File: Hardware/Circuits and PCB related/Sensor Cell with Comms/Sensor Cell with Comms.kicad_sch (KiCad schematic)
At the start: 5 parts, among them U1 TCAN337

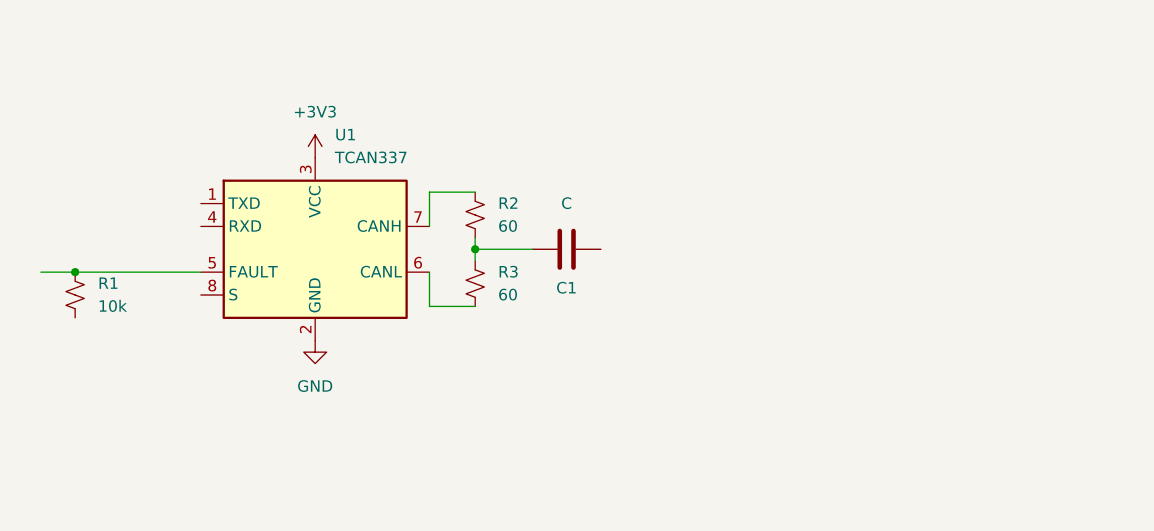
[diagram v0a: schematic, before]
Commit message: TCAN337 Wiring diagram redone to include the componenent sizing for the pcb stage
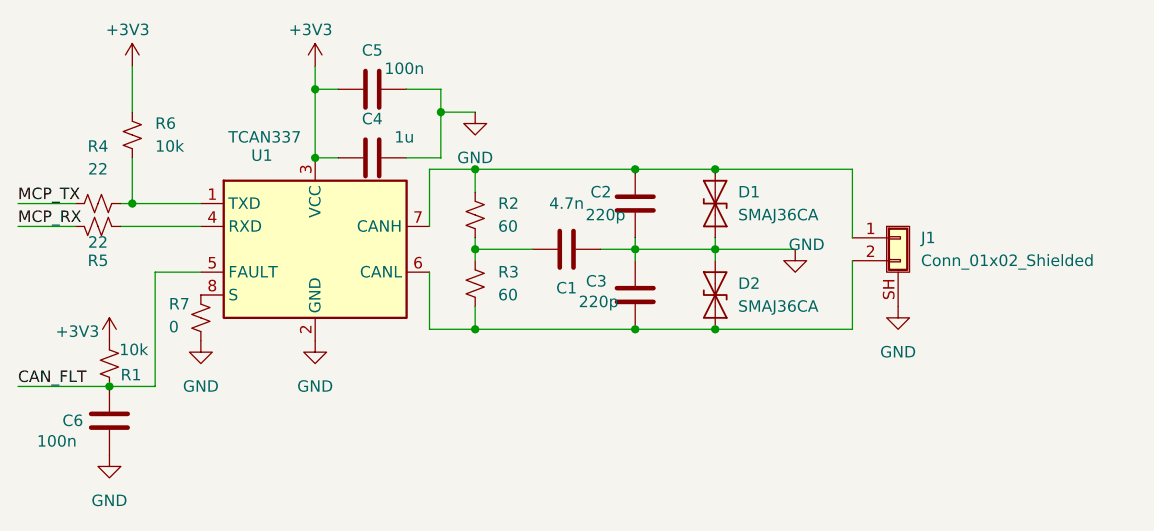
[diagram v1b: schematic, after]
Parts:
- added C2, C3: 220p, Capacitor_SMD:C_0603_1608Metric_Pad1.08x0.95mm_HandSolder, symbol Device:C
- added C4: 1u, Capacitor_SMD:C_0603_1608Metric_Pad1.08x0.95mm_HandSolder, symbol Device:C
- added C5, C6: 100n, Capacitor_SMD:C_0603_1608Metric_Pad1.08x0.95mm_HandSolder, symbol Device:C
- added D1, D2: SMAJ36CA, Diode_SMD:D_SMA, symbol Diode:SMAJ36CA
- added J1: Conn_01x02_Shielded, symbol Connector_Generic_Shielded:Conn_01x02_Shielded
- added R4, R5: 22, Resistor_SMD:R_0603_1608Metric_Pad0.98x0.95mm_HandSolder, symbol Device:R_Small_US
- added R6: 10k, Resistor_SMD:R_0603_1608Metric_Pad0.98x0.95mm_HandSolder, symbol Device:R_Small_US
- added R7: 0, Resistor_SMD:R_0603_1608Metric_Pad0.98x0.95mm_HandSolder, symbol Device:R_Small_US
- C1: value C -> 4.7n
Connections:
- net +3V3: now also R1.1, C4.2, C5.2, R6.2
- net GND: now also C1.2, C2.1, C3.2, C4.1, C5.1, C6.1, D1.1 (A1), D2.2 (A2), J1.SH (Shield), R7.1
- net at R2.1, U1.7 (CANH): now also C2.2, D1.2 (A2), J1.1 (Pin_1)
- net CAN_FLT: now reaches R1.2, U1.5 (FAULT)
- net CAN_FLT: now also C6.2
- net at R3.2, U1.6 (CANL): now also C3.1, D2.1 (A1), J1.2 (Pin_2)
- net at U1.1 (TXD): now also R4.1, R6.1
- net at U1.4 (RXD): now also R5.2
- net at U1.8 (S): now also R7.2
- new net MCP_RX: R5.1
- new net MCP_TX: R4.2
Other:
- moved on the sheet: R1

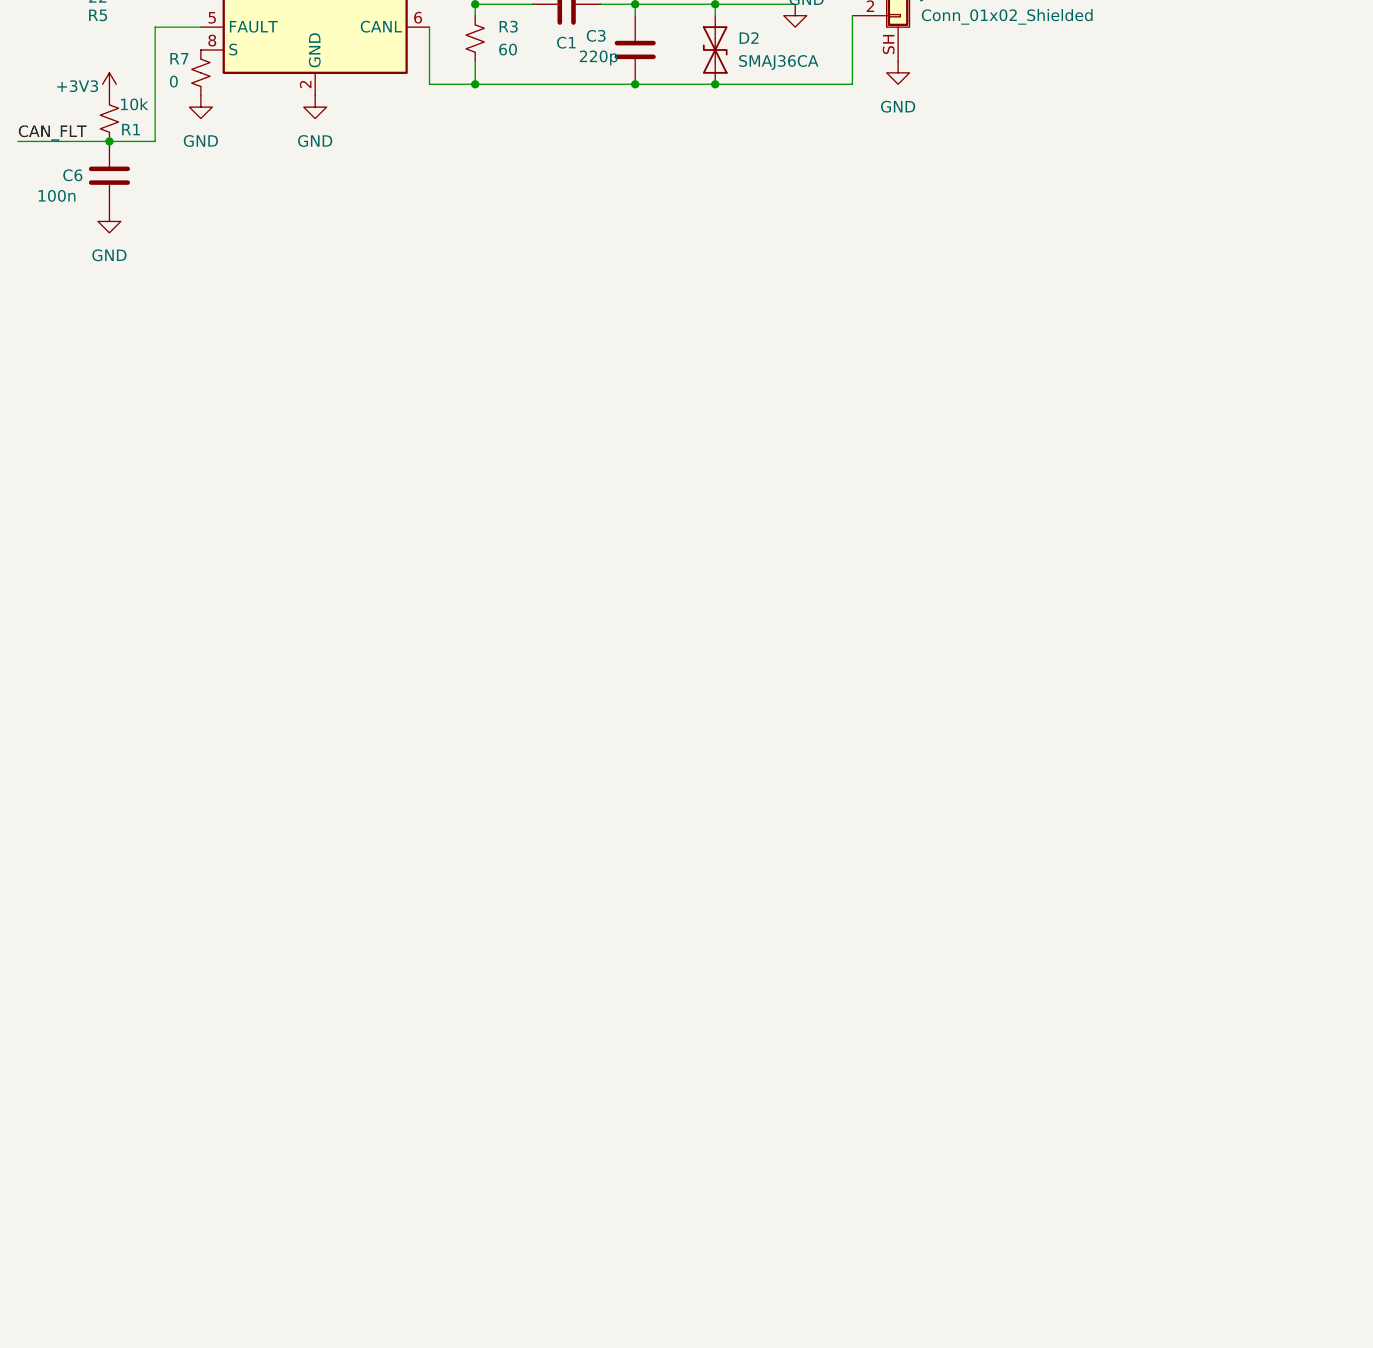
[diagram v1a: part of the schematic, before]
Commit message: need to finish TPS22950x model and wiring but good now for the rest. After wiring diag is done finish actual wiring and move onto PCB process
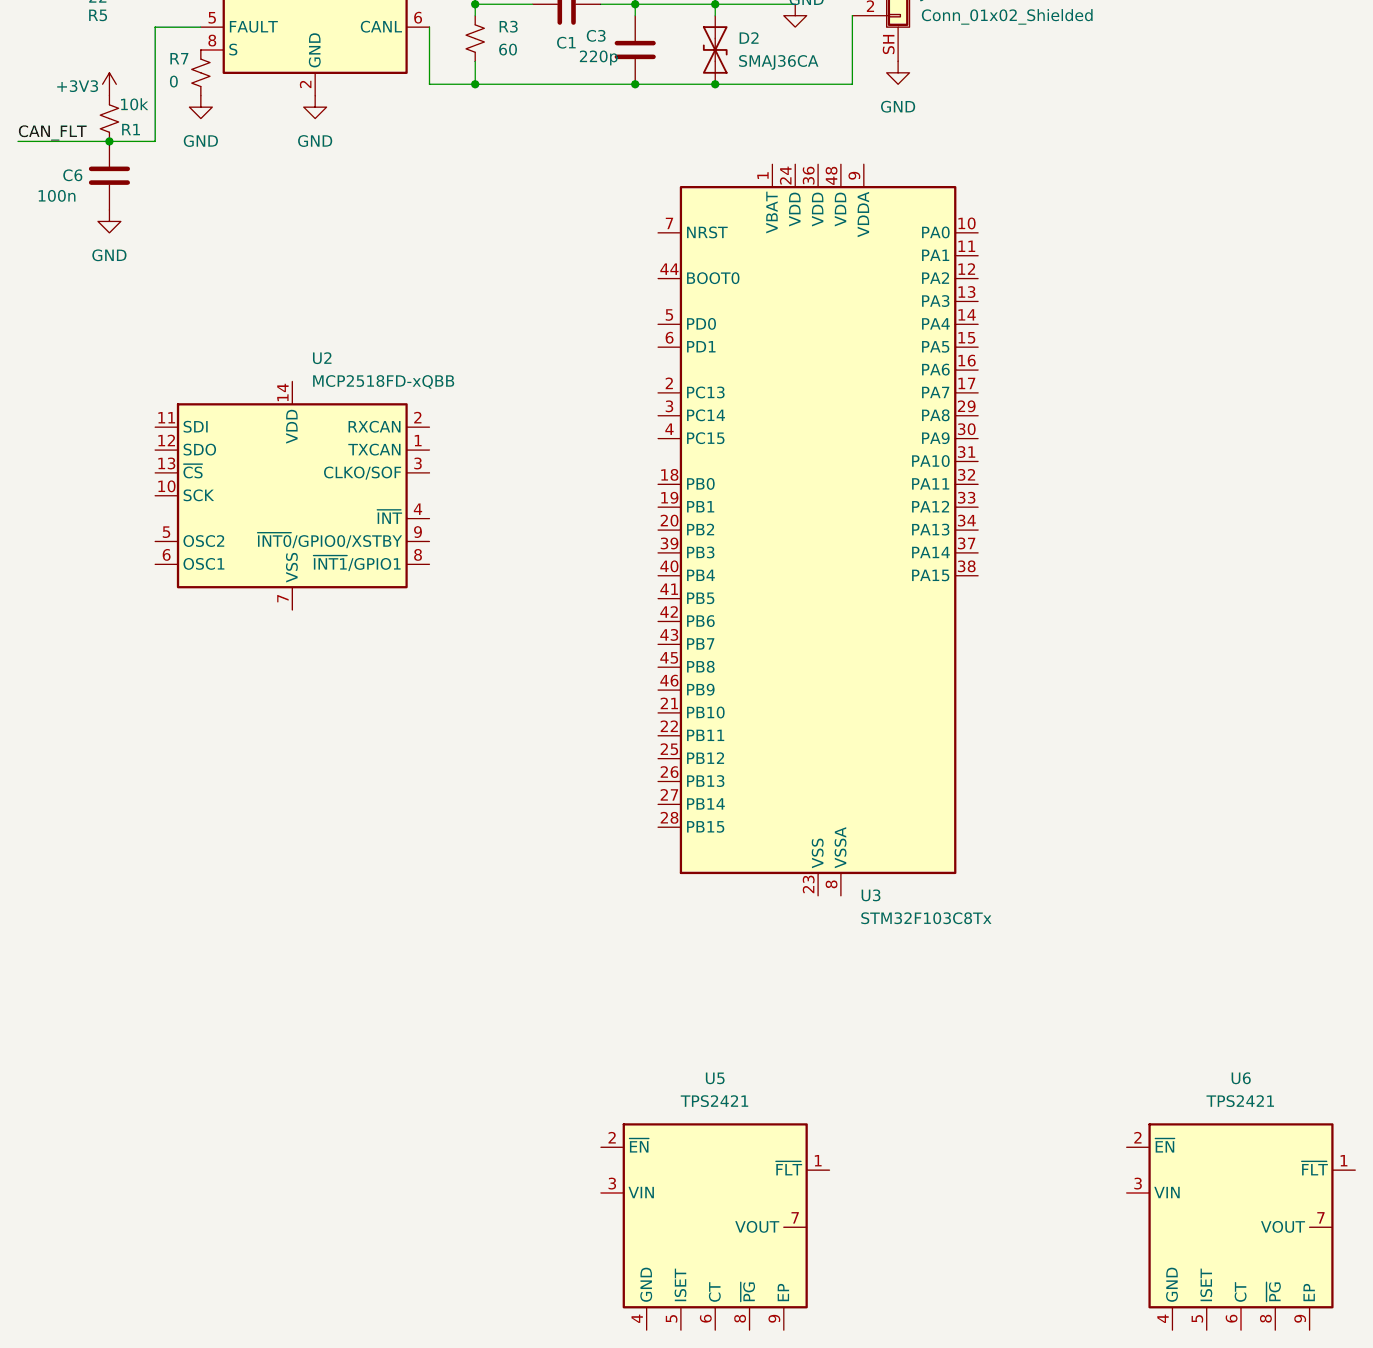
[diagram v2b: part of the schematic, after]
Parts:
- added U2: MCP2518FD-xQBB, Package_SO:SOIC-14_3.9x8.7mm_P1.27mm, symbol Interface_CAN_LIN:MCP2518FD-xQBB
- added U3: STM32F103C8Tx, Package_QFP:LQFP-48_7x7mm_P0.5mm, symbol MCU_ST_STM32F1:STM32F103C8Tx
- added U5, U6: TPS2421, Package_SO:HSOP-8-1EP_3.9x4.9mm_P1.27mm_EP2.41x3.1mm_ThermalVias, symbol Custom Power:TPS2421
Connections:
- new net: U2.15 (VSS), U2.7 (VSS)
- new net: U3.23 (VSS), U3.35 (VSS), U3.47 (VSS)

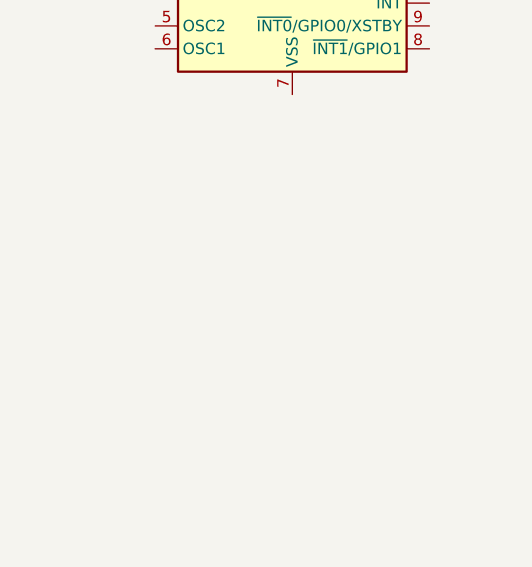
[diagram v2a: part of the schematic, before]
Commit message: TPS22950x model done and included
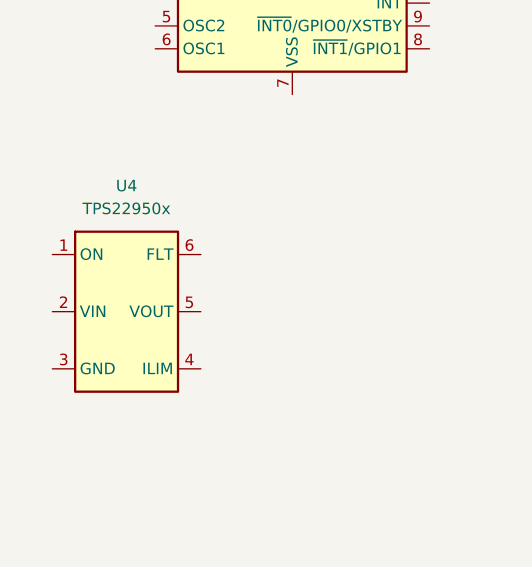
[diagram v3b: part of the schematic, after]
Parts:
- added U4: TPS22950x, Package_TO_SOT_SMD:SOT-23-6, symbol Custom Power:TPS22950x
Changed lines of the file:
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@@
+	)
+	(symbol
+		(lib_id "Custom Power:TPS22950x")
+		(at 25.4 124.46 0)
+		(unit 1)
+		(exclude_from_sim no)
+		(in_bom yes)
+		(on_board yes)
+		(dnp no)
+		(fields_autoplaced yes)
+		(property "Reference" "U4"
+			(at 24.765 115.57 0)
+			(effects
+				(font
+					(size 1.27 1.27)
+				)
+			)
+		)
+		(property "Value" "TPS22950x"
+			(at 24.765 118.11 0)
+			(effects
+				(font
+					(size 1.27 1.27)
+				)
+			)
+		)
+		(property "Footprint" "Package_TO_SOT_SMD:SOT-23-6"
+			(at 25.4 142.24 0)
+			(effects
+				(font
+					(size 1.27 1.27)
+				)
+				(hide yes)
+			)
+		)
+		(property "Datasheet" "http://www.ti.com/lit/ds/symlink/tps22810.pdf"
+			(at 25.908 110.744 0)
+			(effects
+				(font
+					(size 1.27 1.27)
+				)
+				(hide yes)
+			)
+		)
+		(property "Description" "2.7..18V, 2A, 79mohms On-Resistance Load Switch With Thermal Protection, SOT-23-6"
+			(at 25.4 108.712 0)
+			(effects
+				(font
+					(size 1.27 1.27)
+				)
+				(hide yes)
+			)
+		)
+		(pin "6"
+		)
+		(pin "3"
+		)
+		(pin "4"
+		)
+		(pin "2"
+		)
+		(pin "1"
+		)
+		(pin "5"
+		)
+		(instances
+			(project ""
+				(path "/953799b5-f11e-4770-941d-f5d23acc5c6d"
+					(reference "U4")
+					(unit 1)
+				)
+			)
+		)
 	)
 	(symbol
